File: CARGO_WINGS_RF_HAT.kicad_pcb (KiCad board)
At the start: 2 copper layers, 65 x 30 mm, 12 parts, among them J1 RPi_GPIO, J2 ESP Prog, J3 Conn_01x04_Socket, J4 Conn_01x04_Socket, J5 S2B-PH-K-S(LF)(SN), U1 DWM1000, U2 ESP32-S3-WROOM-1-N8R2

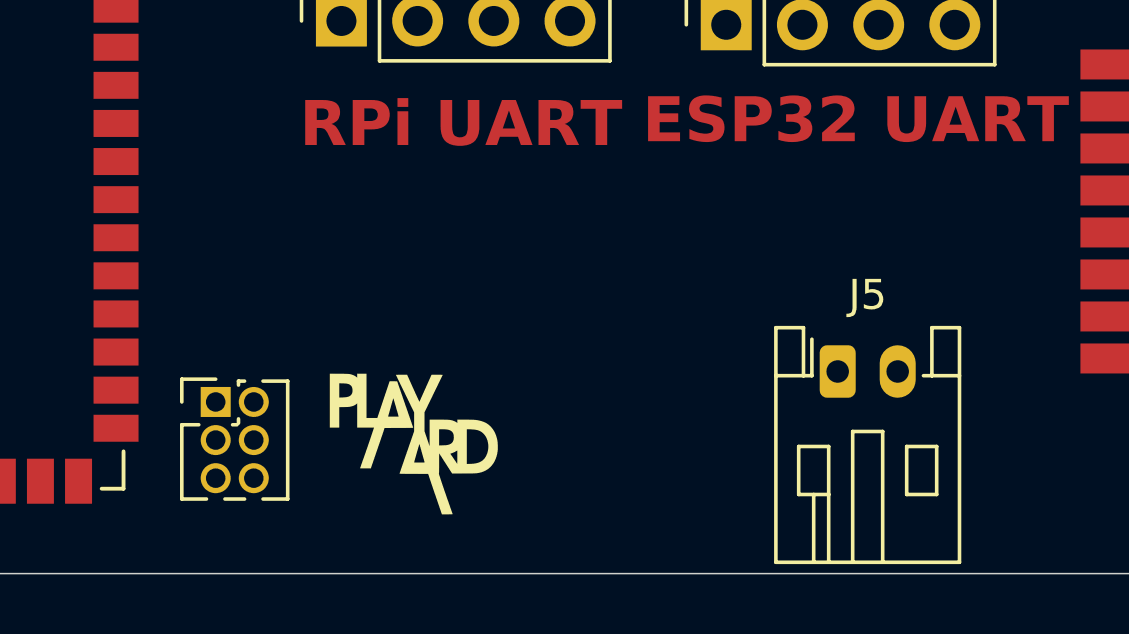
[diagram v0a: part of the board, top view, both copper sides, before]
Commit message: Update
- smps added
- booster added 3.7V to 5V
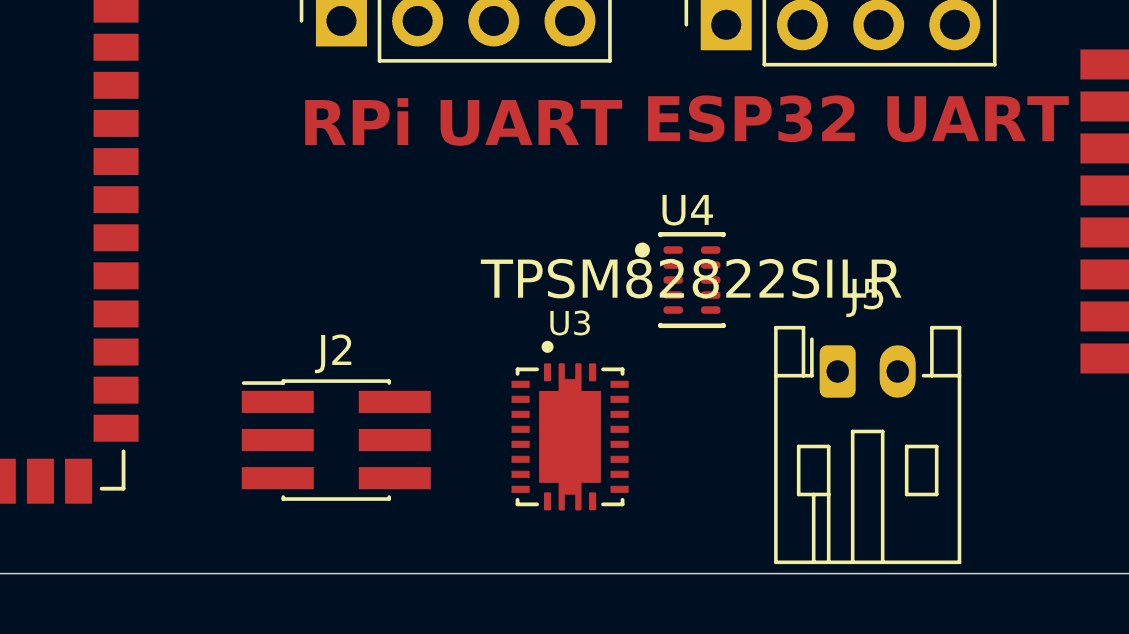
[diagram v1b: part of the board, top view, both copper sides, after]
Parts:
- added U3: TPS61088RHLT, IC_MSP430FR2522IRHLR:IC_MSP430FR2522IRHLR, F.Cu at (83.7, 74.4)
- added U4: TPSM82822SILR, Texas_Instruments-SIL0010D-0-0-MFG:Texas_Instruments-SIL0010D-0-0-MFG, F.Cu at (87.8, 69.2)
- G***: moved to B.Cu
- J2: footprint Connector_PinHeader_1.27mm:PinHeader_2x03_P1.27mm_Vertical -> Connector_PinHeader_1.27mm:PinHeader_2x03_P1.27mm_Vertical_SMD
- moved G*** 6.76 mm to (74.2, 69.5), turned to 180 degrees
- moved J2 4.21 mm to (75.9, 74.5)
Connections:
- J5 pad 1: unconnected-(J5-Pin_1-Pad1) -> +BATT
- J5 pad 2: unconnected-(J5-Pin_2-Pad2) -> GND
